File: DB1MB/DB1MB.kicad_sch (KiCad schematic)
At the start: 22 parts, among them J1 Conn_01x10_Socket, J2 Conn_01x10_Socket, J3 Conn_01x10_Socket, J4 Conn_01x10_Socket, J5 Conn_01x10_Socket, J6 Conn_01x10_Socket, U1 MC68331, U2 ATmega48V-10A, U3 CY62157, U4 74LS573, U5 74LS245

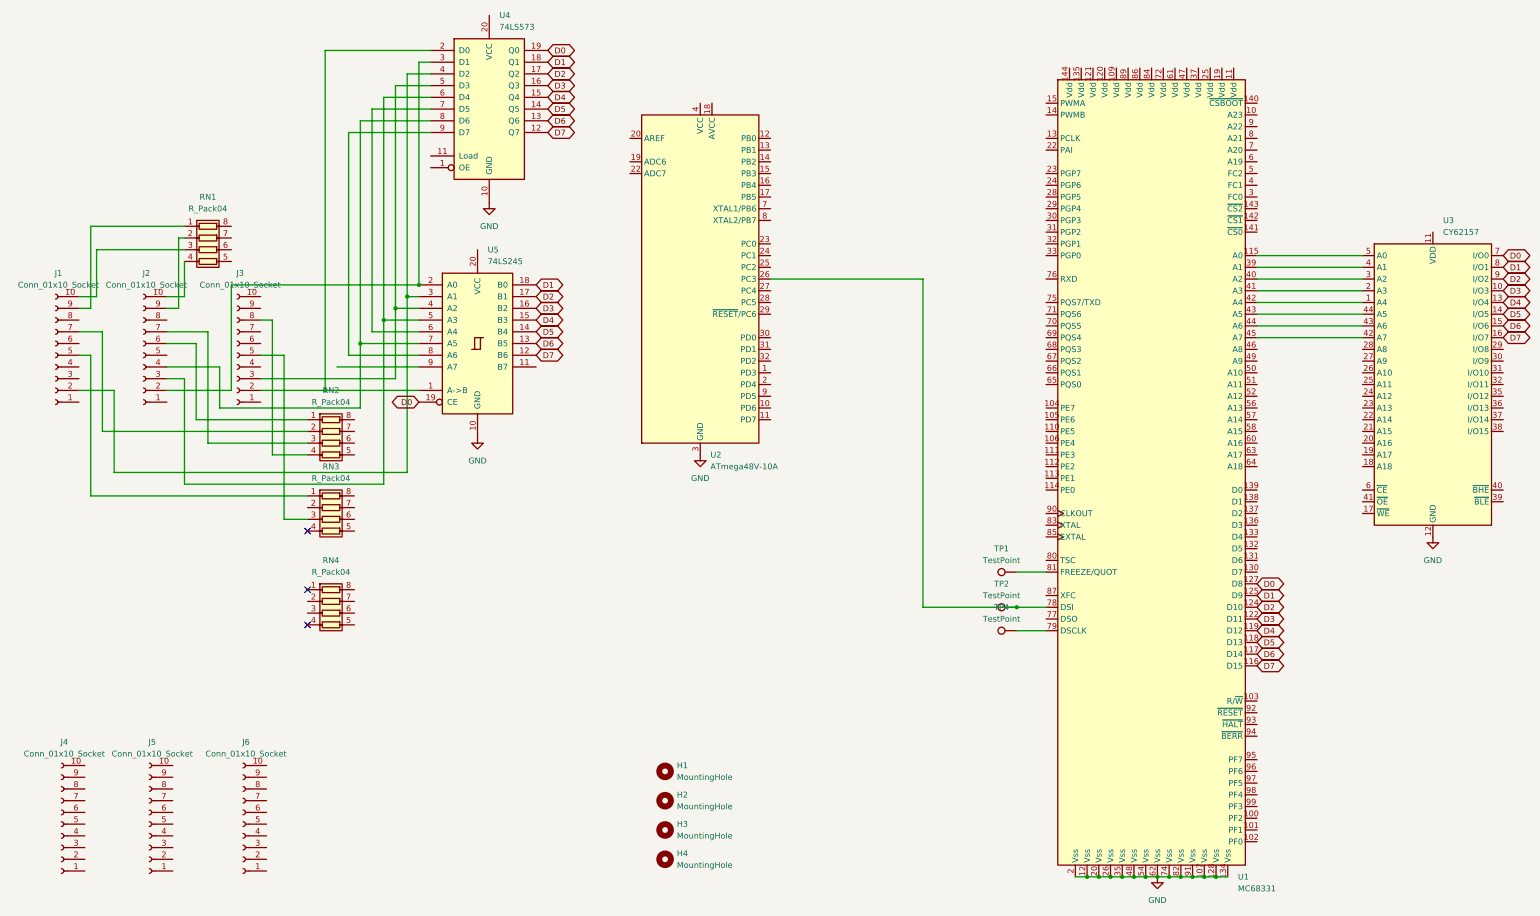
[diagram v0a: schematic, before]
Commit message: vss vdd vertauscht
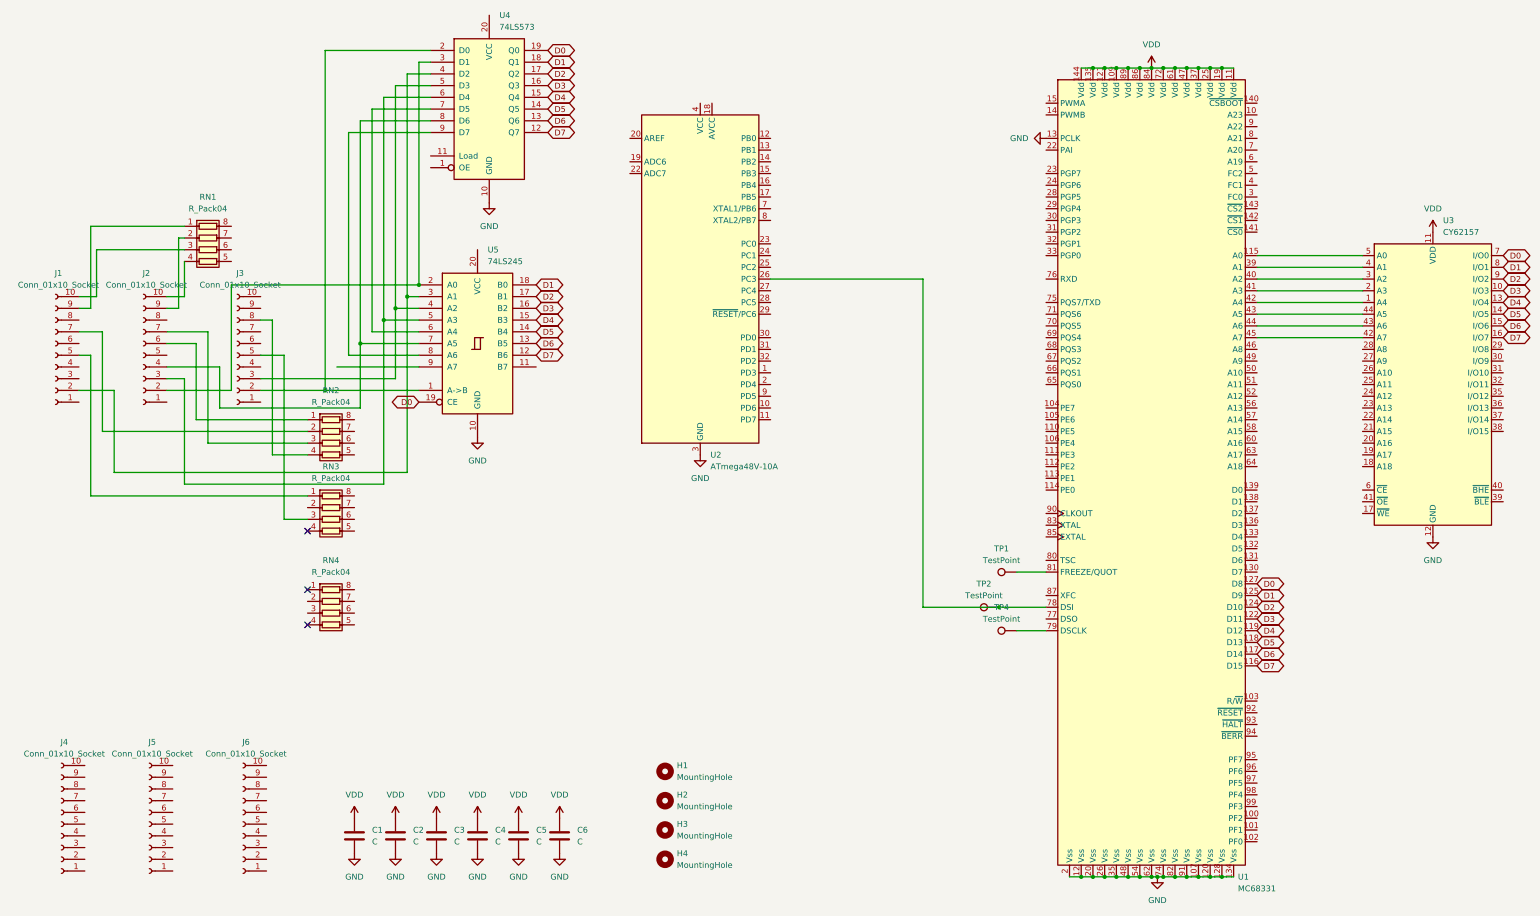
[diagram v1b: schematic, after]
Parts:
- added C1, C2, C3, C4, C5, C6: C, Capacitor_SMD:C_0805_2012Metric, symbol Device:C
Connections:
- net GND: now also U1.120 (Vss), U1.13 (PCLK), C1.2, C2.2, C3.2, C4.2, C5.2, C6.2
- net VDD: now reaches U3.11 (VDD), U3.33 (VDD)
- net VDD: now also U1.109 (Vdd), U1.11 (Vdd), U1.121 (Vdd), U1.135 (Vdd), U1.144 (Vdd), U1.19 (Vdd), U1.25 (Vdd), U1.37 (Vdd), U1.47 (Vdd), U1.61 (Vdd), U1.72 (Vdd), U1.84 (Vdd), U1.86 (Vdd), U1.89 (Vdd), C1.1, C2.1, C3.1, C4.1, C5.1, C6.1
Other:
- moved on the sheet: TP2
